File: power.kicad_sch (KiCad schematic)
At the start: 44 parts, among them J1 KYCON_KPJX-4S-S, J2 MicroFit_2x02, J3 24V/5A OUT, J3B1 DNI, Q1 BC847, Q2 IRF9540SPBF, Q3 BC857, SW1 DNI, U1 MC78M12CDT-TR, U2 MAX5035BUSA

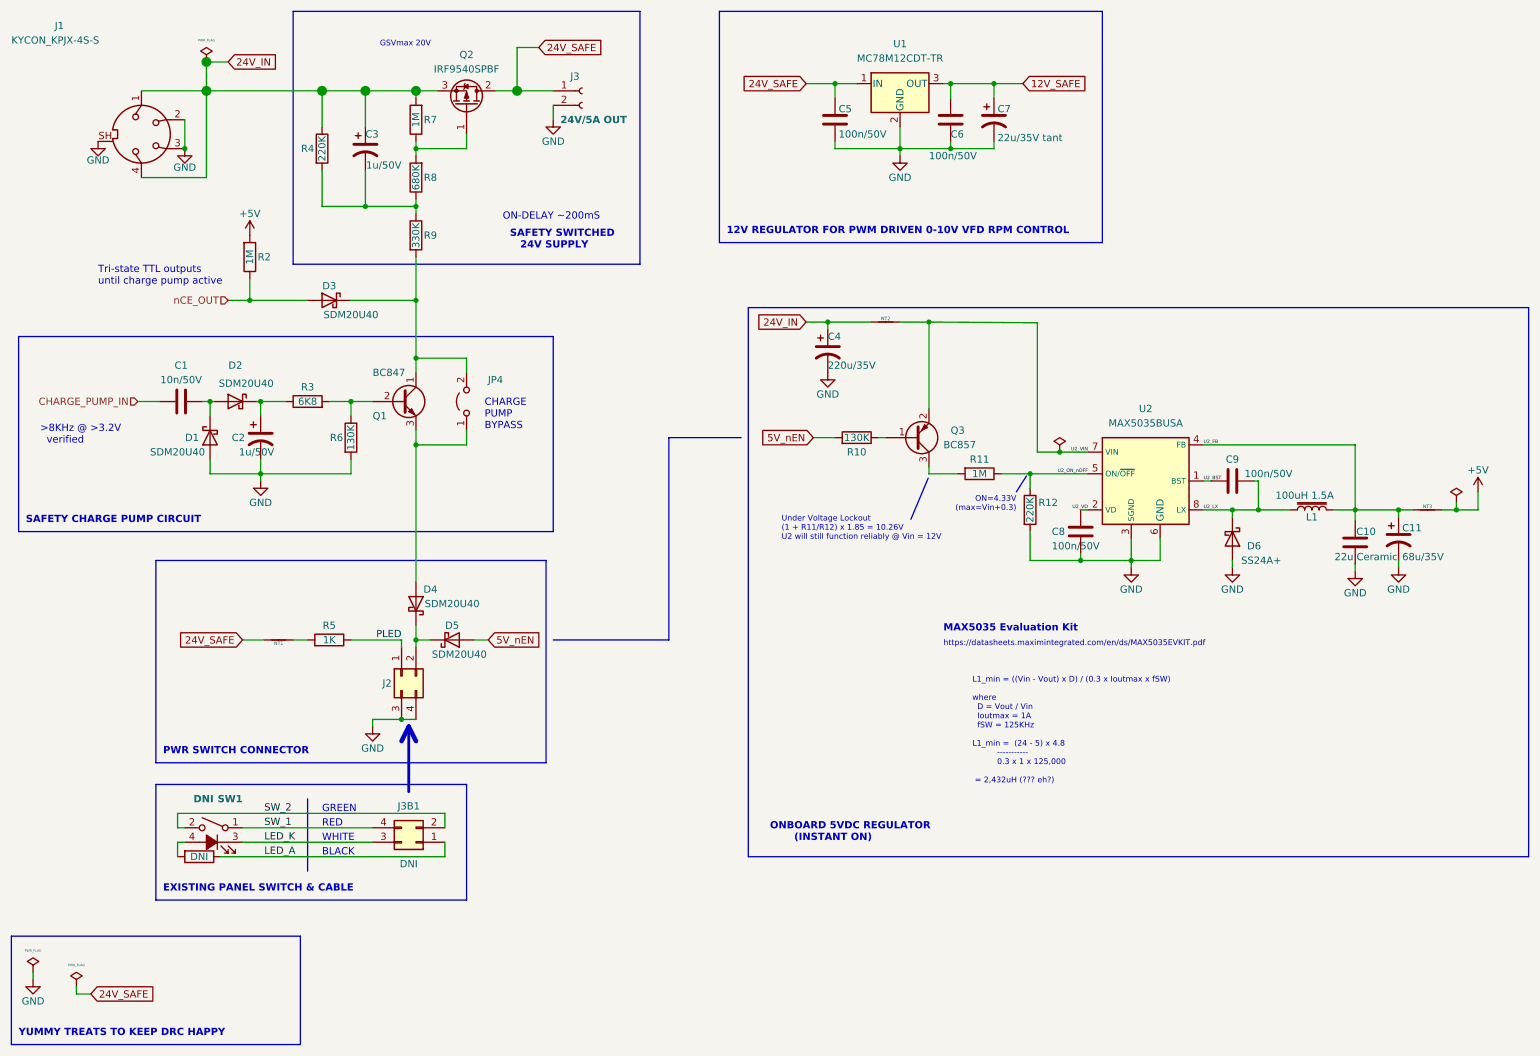
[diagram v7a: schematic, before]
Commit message: Completed change to screw terminal blocks. (P16/17 remains JST.)
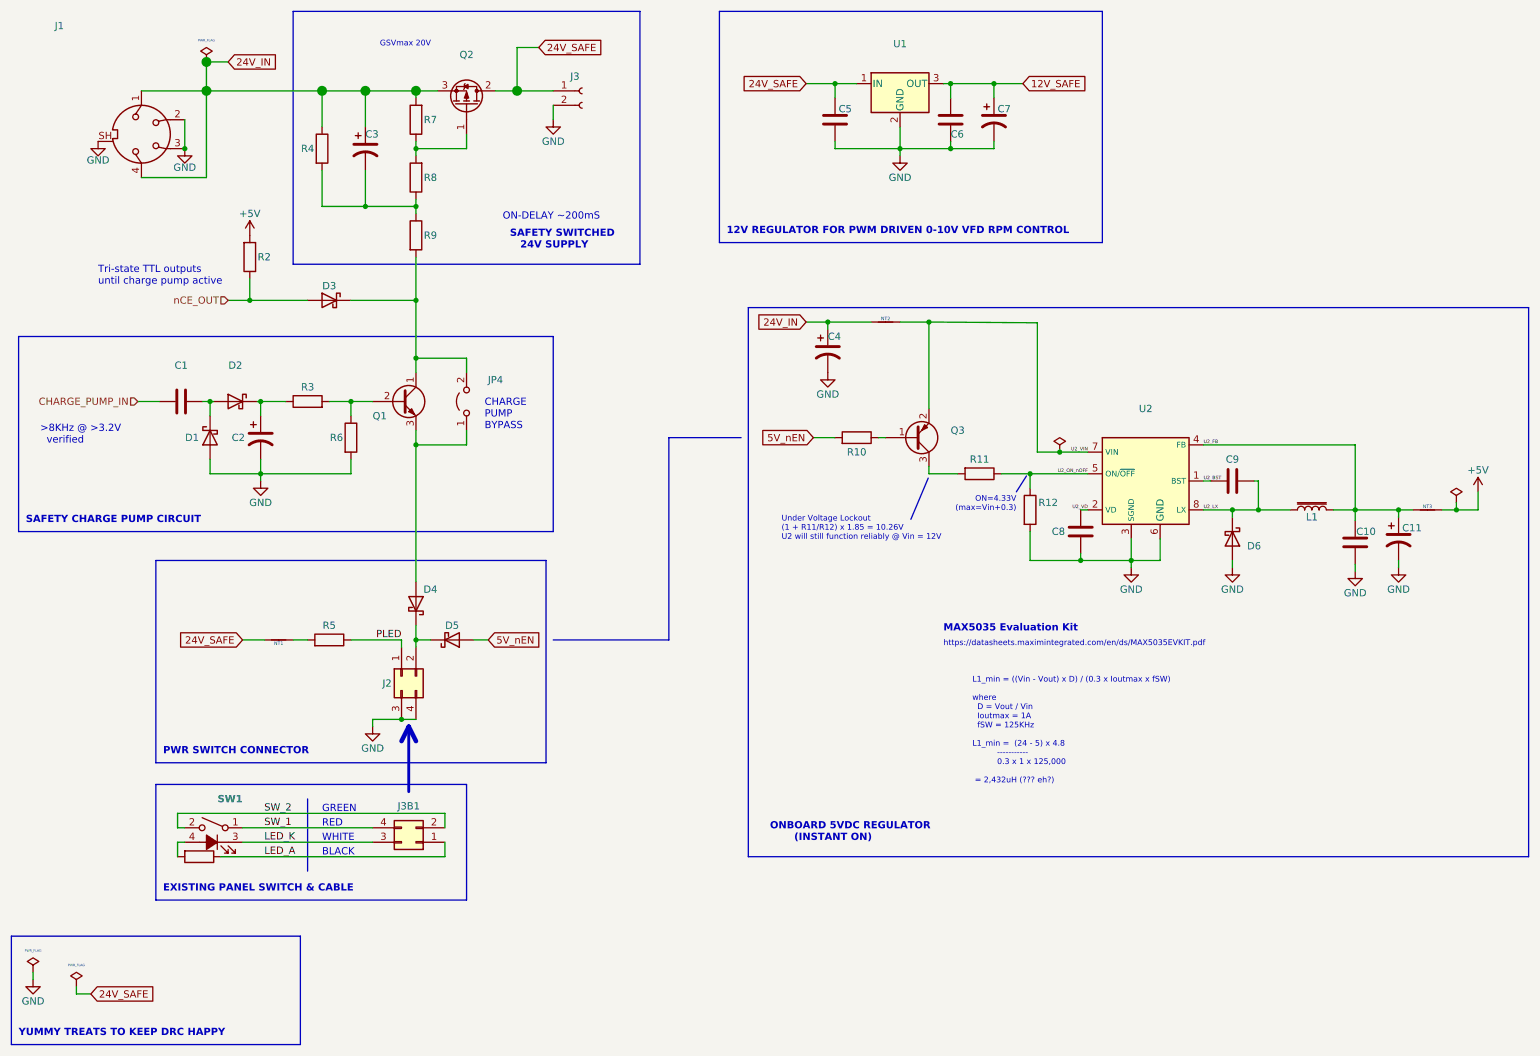
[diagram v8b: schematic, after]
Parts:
- C1: value 10n/50V -> (none); footprint Capacitor_SMD:C_0603_1608Metric -> (none)
- C10: value 22u Ceramic -> (none); footprint Capacitor_SMD:C_1206_3216Metric -> (none)
- C11: value 68u/35V -> (none); footprint -Project:CP_Elec_6.3x7.7_DOT -> (none)
- C2, C3: value 1u/50V -> (none); footprint Capacitor_SMD:C_0603_1608Metric -> (none)
- C4: value 220u/35V -> (none); footprint -Project:CP_Elec_8x10.5_DOT -> (none)
- C5, C6, C8, C9: value 100n/50V -> (none); footprint Capacitor_SMD:C_0603_1608Metric -> (none)
- C7: value 22u/35V tant -> (none); footprint Capacitor_Tantalum_SMD:CP_EIA-7343-31_Kemet-D -> (none)
- D1, D2, D3, D4, D5: value SDM20U40 -> (none); footprint Diode_SMD:D_SOD-523 -> (none)
- D6: value SS24A+ -> (none); footprint -Project:D_SMA_DOT -> (none)
- J1: value KYCON_KPJX-4S-S -> (none); footprint -Project:KYCON_KPJX-4S-S -> (none)
- J2: value MicroFit_2x02 -> (none); footprint Connector_Molex:Molex_Micro-Fit_3.0_43045-0412_2x02_P3.00mm_Vertical -> (none)
- J3: value 24V/5A OUT -> (none); footprint TerminalBlock_RND:TerminalBlock_RND_205-00232_1x02_P5.08mm_Horizontal -> (none)
- J3B1, SW1: value DNI -> (none)
- JP4: value Jumper_2_Bridged -> (none); footprint Connector_PinHeader_2.54mm:PinHeader_2x01_P2.54mm_Vertical -> (none)
- L1: value 100uH 1.5A -> (none); footprint Inductor_SMD:L_12x12mm_H6mm -> (none)
- NT1: value DNI -> (none); footprint -Project:NetTie-2_SMD_Pad0.3mm -> (none)
- NT2, NT3: value DNI -> (none); footprint -Project:NetTie-2_SMD_Pad1.0mm -> (none)
- Q1: value BC847 -> (none); footprint -Project:SOT-23_DOT -> (none)
- Q2: value IRF9540SPBF -> (none); footprint Package_TO_SOT_SMD:TO-263-2 -> (none)
- Q3: value BC857 -> (none); footprint -Project:SOT-23_DOT -> (none)
- R1: value DNI -> (none); footprint Resistor_SMD:R_0603_1608Metric -> (none)
- R10, R6: value 130K -> (none); footprint Resistor_SMD:R_0603_1608Metric -> (none)
- R11, R2, R7: value 1M -> (none); footprint Resistor_SMD:R_0603_1608Metric -> (none)
- R12, R4: value 220K -> (none); footprint Resistor_SMD:R_0603_1608Metric -> (none)
- R3: value 6K8 -> (none); footprint Resistor_SMD:R_0603_1608Metric -> (none)
- R5: value 1K -> (none); footprint Resistor_SMD:R_0603_1608Metric -> (none)
- R8: value 680K -> (none); footprint Resistor_SMD:R_0603_1608Metric -> (none)
- R9: value 330K -> (none); footprint Resistor_SMD:R_0603_1608Metric -> (none)
- U1: value MC78M12CDT-TR -> (none); footprint Package_TO_SOT_SMD:TO-252-2 -> (none)
- U2: value MAX5035BUSA -> (none); footprint Package_SO:SOIC-8_3.9x4.9mm_P1.27mm -> (none)
